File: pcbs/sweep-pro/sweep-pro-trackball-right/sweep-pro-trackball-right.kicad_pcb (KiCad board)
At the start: 2 copper layers, 115 x 86.7 mm, 47 parts, among them J1 Conn_01x07_Male, J2 expantion1, SW1 SW_PUSH-kbd, SW10 SW_PUSH-kbd, SW11 SW_PUSH-kbd, SW12 SW_PUSH-kbd, SW13 SW_PUSH-kbd, SW14 SW_PUSH-kbd, SW15 SW_PUSH-kbd, SW16 SW_PUSH-kbd, SW17 SW_PUSH-kbd, SW2 SW_PUSH-kbd, SW3 SW_PUSH-kbd, SW4 SW_PUSH-kbd, SW5 SW_PUSH-kbd, SW6 SW_PUSH-kbd, SW7 SW_PUSH-kbd, SW8 SW_PUSH-kbd, SW9 SW_PUSH-kbd, U1 ProMicro-kbd

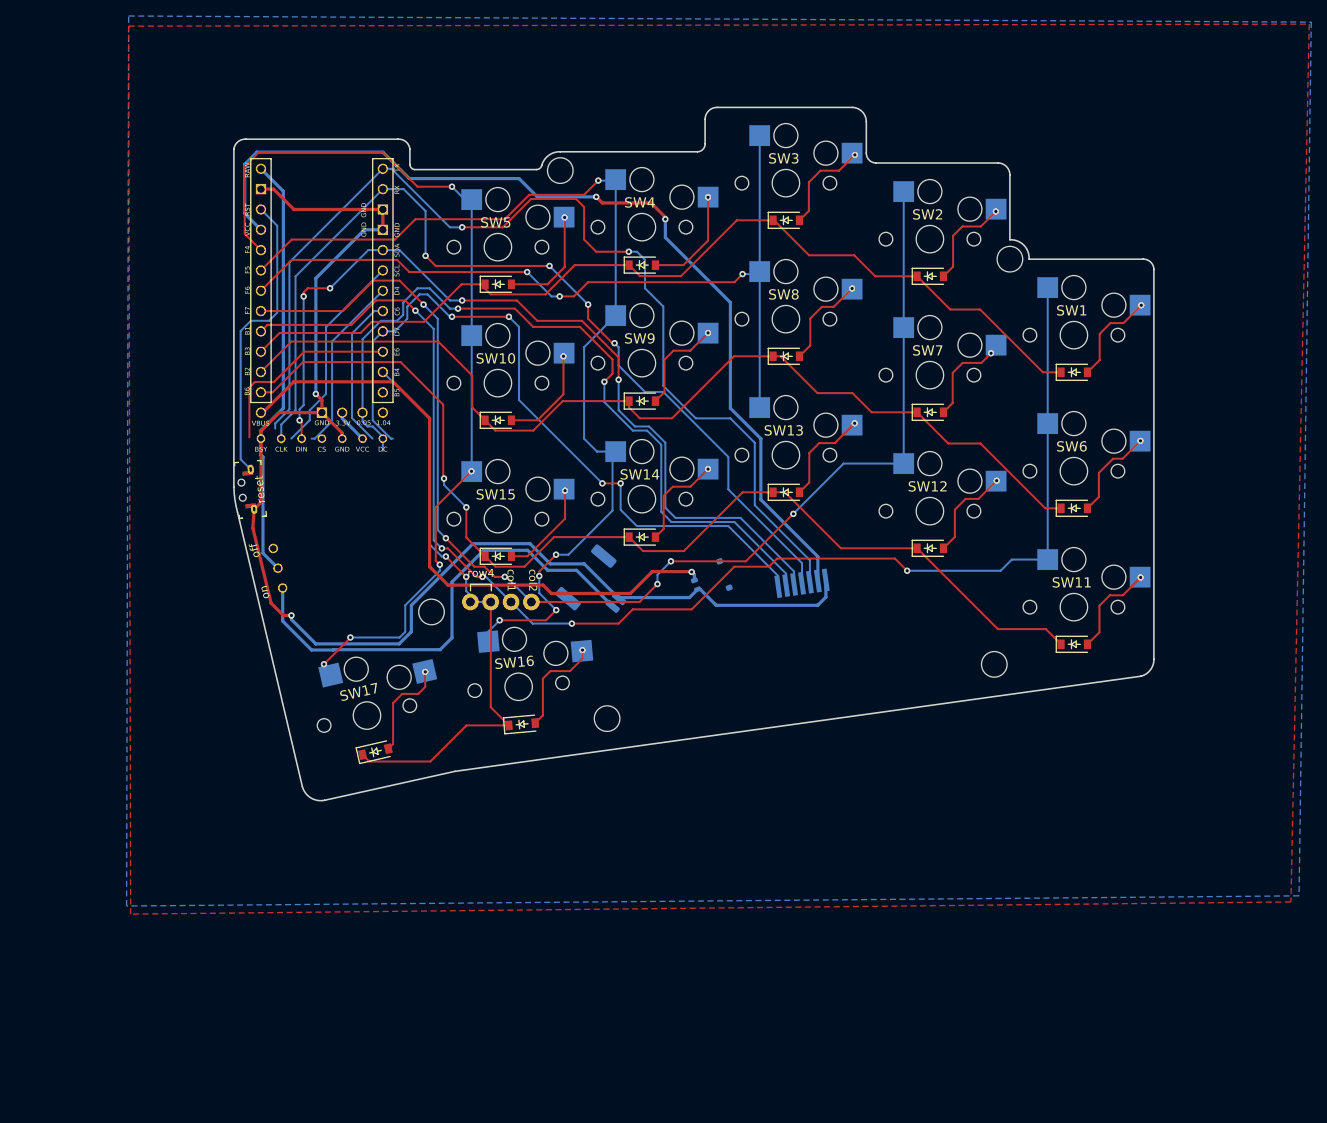
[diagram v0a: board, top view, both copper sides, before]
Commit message: init version with integrated trackball in thumb position
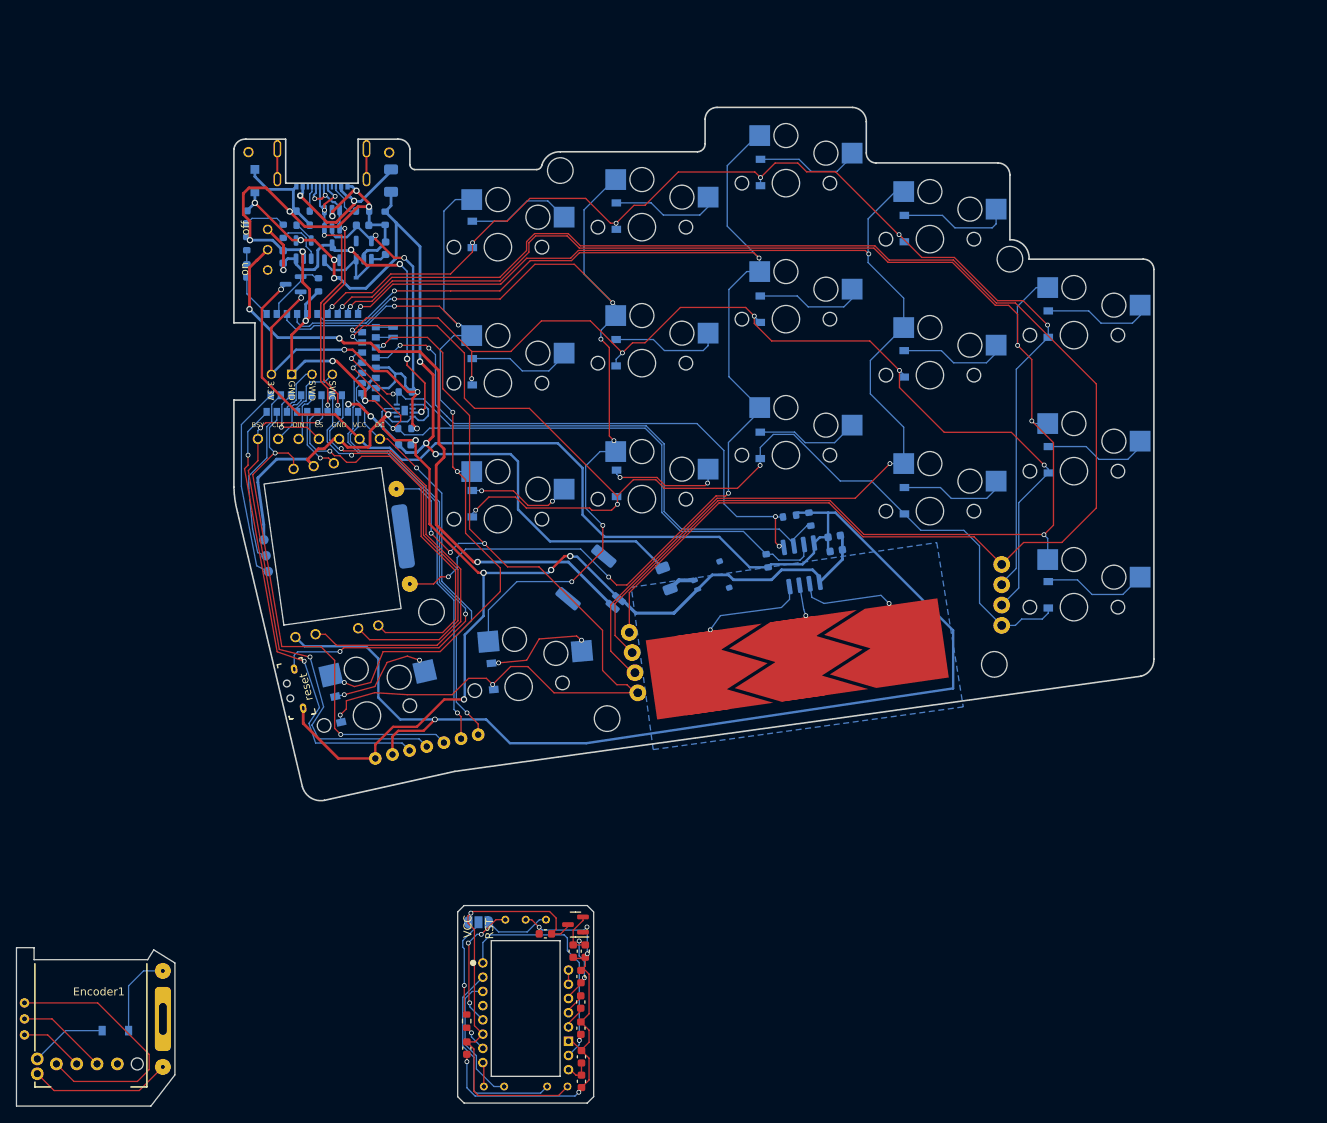
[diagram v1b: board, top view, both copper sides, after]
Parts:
- removed Display1: Conn_Display_general, mylib:Conn_LCD
- removed SW_Power1: SW_Battery-kbd, mylib:SW_BSI10
- added C1: 4.7u, Capacitor_SMD:C_0603_1608Metric, B.Cu at (98.2, 78.2)
- added C10: 1u, Capacitor_SMD:C_0603_1608Metric, F.Cu at (119.3, 141.5)
- added C11: 100n, Capacitor_SMD:C_0603_1608Metric, F.Cu at (106.0, 153.6)
- added C12: 10u (X7R), Capacitor_SMD:C_0603_1608Metric, F.Cu at (120.3, 157.8)
- added C13: 10n (X7R), Capacitor_SMD:C_0603_1608Metric, F.Cu at (120.3, 154.7)
- added C14: 0.1uF, Capacitor_SMD:C_0603_1608Metric, B.Cu at (152.2, 91.5)
- added C15: 1uF, Capacitor_SMD:C_0603_1608Metric, B.Cu at (151.9, 89.7)
- added C2: 10u, Capacitor_SMD:C_0603_1608Metric, B.Cu at (95.8, 53.7)
- added C3: 4.7u, Capacitor_SMD:C_0603_1608Metric, B.Cu at (93.0, 50.8)
- added C4: 0.1u, Capacitor_SMD:C_0603_1608Metric, B.Cu at (83.0, 54.8)
- added C5: 10n, Capacitor_SMD:C_0603_1608Metric, F.Cu at (120.3, 151.2)
- added C6: 100n, Capacitor_SMD:C_0603_1608Metric, F.Cu at (120.8, 141.5)
- added C7: 3.3u/16V, Capacitor_SMD:C_0603_1608Metric, F.Cu at (120.3, 144.7)
- added C8: 100n (X7R), Capacitor_SMD:C_0603_1608Metric, F.Cu at (120.2, 147.9)
- added C9: 1u, Capacitor_SMD:C_0603_1608Metric, F.Cu at (115.8, 139.4)
- added D18: 1N4148W, mylib:Diode, B.Cu at (62.1, 151.5)
- added D19: SMF9.0CA, Diode_SMD:D_SOD-123F, B.Cu at (79.5, 45.2)
- added D20: BAT60B, Diode_SMD:D_SOD-323, B.Cu at (91.1, 57.4)
- added D21: BLUE, LED_SMD:LED_0603_1608Metric, B.Cu at (78.5, 56.5)
- added D22: RED, LED_SMD:LED_0603_1608Metric, B.Cu at (78.5, 49.8)
- added Encoder1: RotaryEncoder, mylib:Panasonic_EVQWGD001_Latest, F.Cu at (60.0, 150.0)
- added F1: 500mA, Fuse:Fuse_1206_3216Metric, B.Cu at (96.5, 45.2)
- added F2: 500mA, Fuse:Fuse_1206_3216Metric, B.Cu at (130.9, 94.9)
- added J10: Conn_01x07, mylib:Magnetic-PogoPin-1x07-Male, B.Cu at (101.0, 116.0)
- added J11: Conn_01x04_Female, Connector_PinHeader_2.54mm:PinHeader_1x04_P2.54mm_Vertical, F.Cu at (89.2, 69.4)
- added J12: USB-C USB 2.0 MC-372, mylib:nrfmicro_USB-C_C168688, B.Cu at (87.9, 45.5)
- added J16: Conn_01x03_Male, mylib:TouchSlider-3_36x10mm, F.Cu at (147.3, 105.0)
- added J3: Conn_01x07, mylib:PMW3610-Ref-Male, F.Cu at (108.0, 143.0)
- added J5: Conn_01x05, mylib:Panasonic_EVQWGD001_Ref_Male, F.Cu at (60.0, 150.0)
- added J9: Conn_Display_general, mylib:Conn_Display_MountHole, F.Cu at (87.5, 77.5)
- added JP1: SolderJumper_3_Open, Jumper:SolderJumper-3_P1.3mm_Open_RoundedPad1.0x1.5mm_NumberLabels, B.Cu at (107.5, 137.9)
- added Q1: AO3407, Package_TO_SOT_SMD:SOT-23, B.Cu at (89.2, 54.2)
- added Q2: AO3407, Package_TO_SOT_SMD:SOT-23, B.Cu at (84.3, 58.2)
- added R1: 5.1K, Resistor_SMD:R_0603_1608Metric, B.Cu at (85.5, 49.0)
- added R10: 10k, Resistor_SMD:R_0603_1608Metric, B.Cu at (143.5, 92.7)
- added R11: 10k, Resistor_SMD:R_0603_1608Metric, B.Cu at (148.9, 87.5)
- added R12: 10k, Resistor_SMD:R_0603_1608Metric, B.Cu at (146.3, 87.1)
- added R13: 2M, Resistor_SMD:R_0603_1608Metric, F.Cu at (106.0, 150.3)
- added R2: 5.1K, Resistor_SMD:R_0603_1608Metric, B.Cu at (93.0, 49.0)
- added R3: 100K, Resistor_SMD:R_0603_1608Metric, B.Cu at (95.8, 49.9)
- added R4: 1K, Resistor_SMD:R_0603_1608Metric, B.Cu at (78.5, 53.1)
- added R5: 2M, Resistor_SMD:R_0603_1608Metric, B.Cu at (87.5, 58.2)
- added R6: 1K, Resistor_SMD:R_0603_1608Metric, B.Cu at (83.0, 51.5)
- added R7: 5K, Resistor_SMD:R_0603_1608Metric, B.Cu at (85.5, 50.8)
- added R8: 5.1k, Resistor_SMD:R_0603_1608Metric, B.Cu at (98.3, 71.6)
- added R9: 5.1k, Resistor_SMD:R_0603_1608Metric, B.Cu at (98.2, 76.2)
- added Ref1: Conn_01x05, mylib:Panasonic_EVQWGD001_Ref, F.Cu at (90.1, 90.8)
- added Ref2: Conn_1x07, mylib:PMW3610-Ref, B.Cu at (92.9, 85.5)
- added SW_Bat1: SW_Battery-kbd, mylib:SW_BSI10, F.Cu at (77.8, 53.8)
- added U2: SRV05-4, mylib:SRV05-4, B.Cu at (89.1, 50.0)
- added U3: XC6220B331MR-G, Package_TO_SOT_SMD:SOT-23-5, B.Cu at (93.1, 53.9)
- added U4: MAX17048, mylib:MAX17048-TDFN-8-1EP_2x2mm_P0.5mm_EP0.8x1.2mm, B.Cu at (98.2, 74.0)
- added U5: TP4054, Package_TO_SOT_SMD:SOT-23-5, B.Cu at (85.6, 53.8)
- added U6: PMW3610, mylib:PMW3610, F.Cu at (108.0, 143.0)
- added U7: MCP1700-1802E-TT, Package_TO_SOT_SMD:SOT-23, F.Cu at (119.6, 138.2)
- added U8: CAP1203, Package_SO:SOIC-8_3.9x4.9mm_P1.27mm, B.Cu at (147.9, 93.2)
- added X1: 32.768 kHz, Crystal:Crystal_SMD_MicroCrystal_CM9V-T1A-2Pin_1.6x1.0mm, B.Cu at (96.8, 64.2)
- D1, D10, D11, D12, D13, D14, D15, D16, D17, D2, D3, D4, D5, D6, D7, D8, D9, SW_Reset1: moved to B.Cu
- J1: value Conn_01x07_Male -> expantion1; footprint mylib:fpc_pad_1x07_p1.0 -> mylib:pogopin_1x4; moved to F.Cu
- J2: value expantion1 -> Conn_01x04_Female
- U1: value ProMicro-kbd -> E73-2G4M08S1C; footprint mylib:ProMacroLite_Partial -> mylib:E73-2G4M08S1C-52840; moved to B.Cu
- moved J2 62.6 mm to (172.8, 97.0), turned to 90 degrees
- moved SW_Reset1 25.9 mm to (82.9, 109.2), turned to -77 degrees
- moved J1 23.3 mm to (126.8, 105.5), turned to -82 degrees
- moved U1 12.5 mm to (95.0, 68.0), turned to 180 degrees
- moved D14 7.44 mm to (124.7, 83.1), turned to 90 degrees
- moved D15 7.33 mm to (106.7, 85.6), turned to 90 degrees
- moved D17 7.05 mm to (89.9, 111.3), turned to 103 degrees
- moved D16 7.02 mm to (109.2, 107.2), turned to 95 degrees
- moved D5 7.02 mm to (106.7, 51.9), turned to 90 degrees
- moved D11 6.99 mm to (178.7, 97.0), turned to 90 degrees
- moved D4 6.93 mm to (124.7, 49.6), turned to 90 degrees
- moved D10 6.88 mm to (106.7, 69.1), turned to 90 degrees
- moved D7 6.88 mm to (160.7, 68.1), turned to 90 degrees
- moved D9 6.87 mm to (124.7, 66.7), turned to 90 degrees
- moved D6 6.87 mm to (178.7, 80.1), turned to 90 degrees
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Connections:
- Bat_main1 pad bat+: VBat -> /mcu/VRAW
- D1 pad 1: row1 -> /keyboard/ROW_1
- D10 pad 1: row2 -> /keyboard/ROW_2
- D11 pad 1: row3 -> /keyboard/ROW_3
- D12 pad 1: row3 -> /keyboard/ROW_3
- D13 pad 1: row3 -> /keyboard/ROW_3
- D14 pad 1: row3 -> /keyboard/ROW_3
- D15 pad 1: row3 -> /keyboard/ROW_3
- D16 pad 1: row4 -> /ROW4
- D17 pad 1: row4 -> /ROW4
- D2 pad 1: row1 -> /keyboard/ROW_1
- D3 pad 1: row1 -> /keyboard/ROW_1
- D4 pad 1: row1 -> /keyboard/ROW_1
- D5 pad 1: row1 -> /keyboard/ROW_1
- D6 pad 1: row2 -> /keyboard/ROW_2
- D7 pad 1: row2 -> /keyboard/ROW_2
- D8 pad 1: row2 -> /keyboard/ROW_2
- D9 pad 1: row2 -> /keyboard/ROW_2
- J1 pad 1: GND -> /keyboard/COL_1
- J1 pad 2: VCC -> /keyboard/COL_2
- J1 pad 3: 0.06 -> /keyboard/COL_3
- J1 pad 4: 0.08 -> /ROW4
- J2 pad 1: col2 -> /keyboard/ROW_3
- J2 pad 2: col1 -> /keyboard/ROW_2
- J2 pad 3: row4 -> /keyboard/ROW_1
- J2 pad 4: row4 -> /keyboard/COL_1
- SW1 pad 1: col1 -> /keyboard/COL_2
- SW10 pad 1: col5 -> /keyboard/COL_6
- SW11 pad 1: col1 -> /keyboard/COL_2
- SW12 pad 1: col2 -> /keyboard/COL_3
- SW13 pad 1: col3 -> /COL4
- SW14 pad 1: col4 -> /keyboard/COL_5
- SW15 pad 1: col5 -> /keyboard/COL_6
- SW16 pad 1: col4 -> /keyboard/COL_5
- SW17 pad 1: col5 -> /keyboard/COL_6
- SW2 pad 1: col2 -> /keyboard/COL_3
- SW3 pad 1: col3 -> /COL4
- SW4 pad 1: col4 -> /keyboard/COL_5
- SW5 pad 1: col5 -> /keyboard/COL_6
- SW6 pad 1: col1 -> /keyboard/COL_2
- SW7 pad 1: col2 -> /keyboard/COL_3
- SW8 pad 1: col3 -> /COL4
- SW9 pad 1: col4 -> /keyboard/COL_5
- SW_Reset1 pad 1: reset -> /mcu/RESET
- U1 pad 1: 0.06 -> /mcu/BLUE_LED
- U1 pad 10: bsy -> /keyboard/COL_3
- U1 pad 11: row4 -> Net-(U1-Pad11)
- U1 pad 12: encoder_b -> /keyboard/ROW_2
- U1 pad 13: row3 -> Net-(U1-Pad13)
- U1 pad 14: row2 -> /keyboard/ROW_3
- U1 pad 15: row1 -> /ROW4
- U1 pad 16: col1 -> /mcu/SDA
- U1 pad 17: col2 -> /touchbar/INT
- U1 pad 18: col3 -> /mcu/SCL
- U1 pad 19: col4 -> /mcu/nRF_VDD
- U1 pad 2: 0.08 -> /mcu/VCC_CTRL
- U1 pad 20: col5 -> /mcu/0.12/hi
- U1 pad 21: VCC -> GND
- U1 pad 22: reset -> /MUX1
- U1 pad 23: GND -> /mcu/nRF_VDD
- U1 pad 24: VRaw -> GND
- U1 pad 25: VBus -> unconnected-(U1-Pad25)
- U1 pad 28: GND -> /mcu/0.15/hi
- U1 pad 29: 3.3V -> /mcu/D-
- U1 pad 3: GND -> /keyboard/COL_6
- U1 pad 30: 0.05 -> /mcu/0.17/hi
- U1 pad 31: encoder_a -> /mcu/D+
- U1 pad 4: GND -> /keyboard/COL_5
- U1 pad 5: 0.15 -> GND
- U1 pad 6: din -> /COL4
- U1 pad 7: clk -> /keyboard/ROW_1
- U1 pad 8: dc -> /keyboard/COL_1
- U1 pad 9: cs -> /keyboard/COL_2
- WirelessCharger1 pad vbus: VBus -> Net-(F2-Pad2)
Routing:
- net /VCC: track 0.00 -> 238.1 mm, vias 0 -> 2
- net /keyboard/COL_2: track 0.00 -> 205.5 mm, vias 0 -> 4
- net /keyboard/COL_1: track 0.00 -> 196.9 mm, vias 0 -> 1
- net col1: track 170.7 -> 0.00 mm, vias 5 -> 0
- net /COL4: track 0.00 -> 161.6 mm, vias 0 -> 5
- net /keyboard/COL_3: track 0.00 -> 160.9 mm, vias 0 -> 3
- net col2: track 155.9 -> 0.00 mm, vias 6 -> 0
- net /keyboard/ROW_1: track 0.00 -> 147.8 mm, vias 0 -> 6
- net /keyboard/ROW_3: track 0.00 -> 144.2 mm, vias 0 -> 4
- net /keyboard/ROW_2: track 0.00 -> 133.9 mm, vias 0 -> 6
- net row3: track 133.4 -> 0.00 mm, vias 2 -> 0
- net 0.06: track 132.2 -> 0.00 mm, vias 2 -> 0
- net /ROW4: track 0.00 -> 126.2 mm, vias 0 -> 6
- net row2: track 122.5 -> 0.00 mm
- net col4: track 122.3 -> 0.00 mm, vias 5 -> 0
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- added copper zone on B.Cu, net GND
- removed copper zone on B.Cu, net (none)
- removed copper zone on F.Cu, net (none)
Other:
- outline, holes or cut-outs redrawn
- board text added: "RST"
- board text added: "VCC"
